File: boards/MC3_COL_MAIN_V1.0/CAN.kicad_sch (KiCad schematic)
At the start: 10 parts, among them J70 CAN, U70 TJA1051T/3

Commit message: User: re-annotated schematic (CAN/F412 parts), drill/place + grid origin at (100,100) saved in the board
Co-Authored-By: Claude Fable 5 <noreply@anthropic.com>
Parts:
- renumbered C70 to C28, C71 to C29, C72 to C30, D70 to D4, FB62 to FB3, J70 to J12, JP70 to JP1, R70 to R31, R71 to R32, U70 to U8

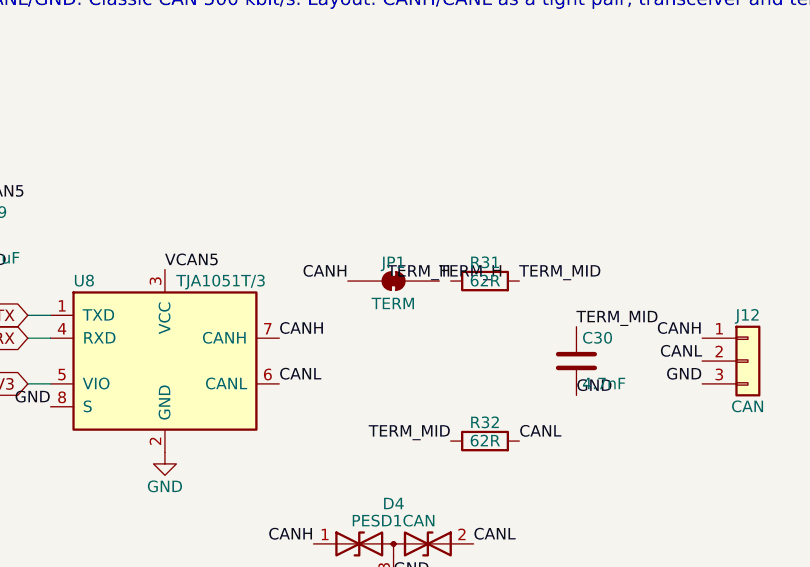
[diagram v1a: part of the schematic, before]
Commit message: CAN: termination enable is a fitted 0R (R72, C17168) instead of the bridged solder jumper (custom-pad footprint not placeable over KiCad 10 IPC)
Co-Authored-By: Claude Fable 5 <noreply@anthropic.com>
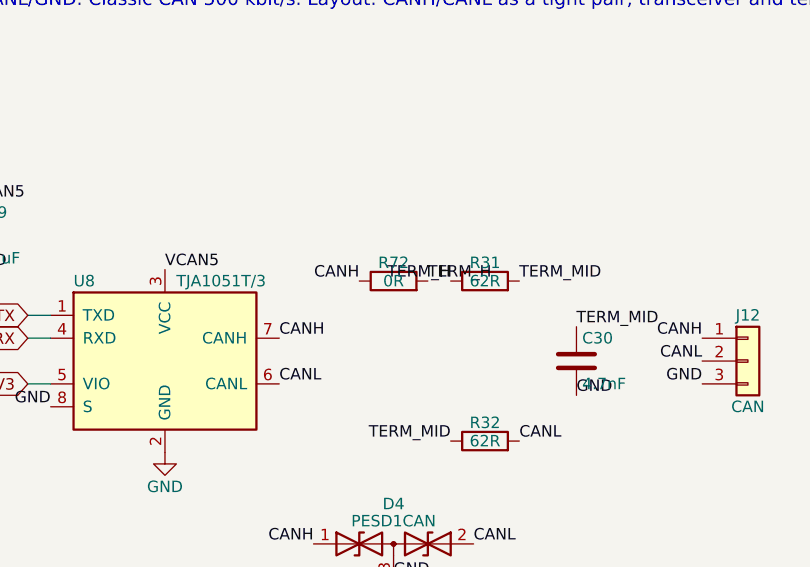
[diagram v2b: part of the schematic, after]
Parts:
- removed JP1: TERM, MC3_COL_MAIN:SolderJumper-2_P1.3mm_Bridged_RoundedPad1.0x1.5mm, symbol Jumper:SolderJumper_2_Bridged
- added R72: 0R, MC3_COL_MAIN:R_0402_1005Metric, symbol Device:R
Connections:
- net CANH: now also R72.1
- net TERM_H: now also R72.2
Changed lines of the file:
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@@
 	(generator_version "10.0")
 	(paper "A4")
-	(text "CAN - machine control link (decision 2026-08-22; vault Control Electronics open item). STM32F412 CAN1 (PA11 RX / PA12 TX) -> TJA1051T/3 -> split termination (2x62R + 4.7nF, solder-jumper JP70 bridged) + PESD1CAN -> pads CANH/CANL/GND. Classic CAN 500 kbit/s. Layout: CANH/CANL as a tight pair, transceiver and termination next to the pads, D70 nearest the pads."
-		(exclude_from_sim no)
-		(at 30 40 0)
-		(effects
-			(font
-				(size 1.5 1.5)
-			)
-		)
-	)
 	(wire
 		(pts
-			(xy 87.63 82.55) (xy 85.09 82.55)
+			(xy 87.63 82.55)
+			(xy 85.09 82.55)
 		)
 		(stroke
@@
 	(wire
 		(pts
-			(xy 87.63 77.47) (xy 85.09 77.47)
+			(xy 87.63 77.47)
+			(xy 85.09 77.47)
 		)
 		(stroke
@@
 	(wire
 		(pts
-			(xy 87.63 74.93) (xy 85.09 74.93)
+			(xy 87.63 74.93)
+			(xy 85.09 74.93)
 		)
 		(stroke
@@
 	(wire
 		(pts
-			(xy 60.96 57.15) (xy 60.96 54.61)
+			(xy 60.96 57.15)
+			(xy 60.96 54.61)
 		)
 		(stroke
@@
 		)
 	)
+	(text "CAN - machine control link (decision 2026-08-22; vault Control Electronics open item). STM32F412 CAN1 (PA11 RX / PA12 TX) -> TJA1051T/3 -> split termination (2x62R + 4.7nF, solder-jumper JP70 bridged) + PESD1CAN -> pads CANH/CANL/GND. Classic CAN 500 kbit/s. Layout: CANH/CANL as a tight pair, transceiver and termination next to the pads, D70 nearest the pads."
+		(at 30 40 0)
+		(effects
+			(font
+				(size 1.5 1.5)
+			)
+		)
+	)
 	(label "TERM_MID"
 		(at 139.7 71.12 0)
@@
 	)
 	(label "TERM_H"
-		(at 130.81 71.12 0)
-		(effects
-			(font
-				(size 1.27 1.27)
-			)
-			(justify left bottom)
-		)
-	)
-	(label "TERM_H"
 		(at 132.08 71.12 180)
 		(effects
@@
 	)
 	(label "CANH"
-		(at 120.65 71.12 180)
-		(effects
-			(font
-				(size 1.27 1.27)
-			)
-			(justify right bottom)
-		)
-	)
-	(label "CANH"
 		(at 116.84 100.33 180)
 		(effects
@@
 	(label "VCAN5"
 		(at 71.12 62.23 0)
+		(effects
+			(font
+				(size 1.27 1.27)
+			)
+			(justify left bottom)
+		)
+	)
+	(label "CANH"
+		(at 121.92 71.12 180)
+		(effects
+			(font
+				(size 1.27 1.27)
+			)
+			(justify right bottom)
+		)
+	)
+	(label "TERM_H"
+		(at 129.54 71.12 0)
 		(effects
 			(font
@@
 		(at 135.89 88.9 90)
 		(unit 1)
-		(body_style 1)
 		(exclude_from_sim no)
 		(in_bom yes)
 		(on_board yes)
-		(in_pos_files yes)
 		(dnp no)
 		(property "Reference" "R32"
@@
 			)
 		)
+		(body_style 1)
+		(in_pos_files yes)
 		(pin "1"
 		)
@@
 		(at 165.1 80.01 0)
 		(unit 1)
-		(body_style 1)
 		(exclude_from_sim no)
 		(in_bom yes)
 		(on_board yes)
-		(in_pos_files yes)
 		(dnp no)
 		(property "Reference" "J12"
@@
 			)
 		)
+		(body_style 1)
+		(in_pos_files yes)
 		(pin "1"
 		)
@@
 		(at 71.12 66.04 0)
 		(unit 1)
-		(body_style 1)
 		(exclude_from_sim no)
 		(in_bom yes)
 		(on_board yes)
-		(in_pos_files yes)
 		(dnp no)
 		(property "Reference" "C28"
@@
 			)
 		)
+		(body_style 1)
+		(in_pos_files yes)
 		(pin "1"
 		)
@@
 		(at 125.73 100.33 0)
 		(unit 1)
-		(body_style 1)
 		(exclude_from_sim no)
 		(in_bom yes)
 		(on_board yes)
-		(in_pos_files yes)
 		(dnp no)
 		(property "Reference" "D4"
@@
 			)
 		)
+		(body_style 1)
+		(in_pos_files yes)
 		(pin "3"
 		)
@@
 		(at 78.74 66.04 0)
 		(unit 1)
-		(body_style 1)
 		(exclude_from_sim no)
 		(in_bom yes)
 		(on_board yes)
-		(in_pos_files yes)
 		(dnp no)
 		(property "Reference" "C29"
@@
 			)
 		)
+		(body_style 1)
+		(in_pos_files yes)
 		(pin "1"
 		)
@@
 	)
 	(symbol
-		(lib_id "Jumper:SolderJumper_2_Bridged")
-		(at 125.73 71.12 0)
+		(lib_id "Device:FerriteBead")
+		(at 60.96 60.96 0)
 		(unit 1)
-		(body_style 1)
 		(exclude_from_sim no)
 		(in_bom yes)
 		(on_board yes)
-		(in_pos_files yes)
-		(dnp no)
-		(property "Reference" "JP1"
-			(at 125.73 69.088 0)
-			(show_name no)
-			(do_not_autoplace no)
-			(effects
-				(font
-					(size 1.27 1.27)
-				)
-			)
-		)
-		(property "Value" "TERM"
-			(at 125.73 73.66 0)
-			(show_name no)
-			(do_not_autoplace no)
-			(effects
-				(font
-					(size 1.27 1.27)
-				)
-			)
-		)
-		(property "Footprint" "MC3_COL_MAIN:SolderJumper-2_P1.3mm_Bridged_RoundedPad1.0x1.5mm"
-			(at 125.73 71.12 0)
-			(hide yes)
-			(show_name no)
-			(do_not_autoplace no)
-			(effects
-				(font
-					(size 1.27 1.27)
-				)
-			)
-		)
-		(property "Datasheet" ""
-			(at 125.73 71.12 0)
-			(hide yes)
-			(show_name no)
-			(do_not_autoplace no)
-			(effects
-				(font
-					(size 1.27 1.27)
-				)
-			)
-		)
-		(property "Description" ""
-			(at 125.73 71.12 0)
-			(show_name no)
-			(do_not_autoplace no)
-			(effects
-				(font
-					(size 1.27 1.27)
-				)
-			)
-		)
-		(property "Note" "Solder jumper, BRIDGED by default = 120R termination fitted. No part"
-			(at 125.73 71.12 0)
-			(hide yes)
-			(show_name no)
-			(do_not_autoplace no)
-			(effects
-				(font
-					(size 1.27 1.27)
-				)
-			)
-		)
-		(pin "1"
-		)
-		(pin "2"
-		)
-		(instances
-			(project "CAN"
-				(path "/3d434ce1-889d-46d1-8950-1c686d039f9f"
-					(reference "JP70")
-					(unit 1)
-				)
-			)
-			(project "MC3_COL_MAIN_V1.0"
-				(path "/7d5f4202-d55e-4c7b-a2df-dd599db38e48/d53768a6-e0ca-46e0-8386-8014881aa541"
-					(reference "JP1")
-					(unit 1)
-				)
-			)
-		)
-	)
-	(symbol
-		(lib_id "Device:FerriteBead")
-		(at 60.96 60.96 0)
-		(unit 1)
-		(body_style 1)
-		(exclude_from_sim no)
-		(in_bom yes)
-		(on_board yes)
-		(in_pos_files yes)
 		(dnp no)
 		(property "Reference" "FB3"
@@
 			)
 		)
+		(body_style 1)
+		(in_pos_files yes)
 		(pin "1"
 		)
@@
 		(at 135.89 71.12 90)
 		(unit 1)
-		(body_style 1)
 		(exclude_from_sim no)
 		(in_bom yes)
 		(on_board yes)
-		(in_pos_files yes)
 		(dnp no)
 		(property "Reference" "R31"
@@
 			)
 		)
+		(body_style 1)
+		(in_pos_files yes)
 		(pin "1"
 		)
@@
 		(at 146.05 80.01 0)
 		(unit 1)
-		(body_style 1)
 		(exclude_from_sim no)
 		(in_bom yes)
 		(on_board yes)
-		(in_pos_files yes)
 		(dnp no)
 		(property "Reference" "C30"
@@
 			)
 		)
+		(body_style 1)
+		(in_pos_files yes)
 		(pin "1"
 		)
@@
 		(at 100.33 90.17 0)
 		(unit 1)
-		(body_style 1)
 		(exclude_from_sim no)
 		(in_bom yes)
 		(on_board yes)
-		(in_pos_files yes)
 		(dnp no)
 		(property "Reference" "#PWR022"
@@
 			)
 		)
+		(body_style 1)
+		(in_pos_files yes)
 		(pin "1"
 		)
@@
 		(at 100.33 80.01 0)
 		(unit 1)
-		(body_style 1)
 		(exclude_from_sim no)
 		(in_bom yes)
 		(on_board yes)
-		(in_pos_files yes)
 		(dnp no)
 		(property "Reference" "U8"
@@
 			)
 		)
+		(body_style 1)
+		(in_pos_files yes)
 		(pin "1"
 		)
@@
 		(at 60.96 64.77 180)
 		(unit 1)
-		(body_style 1)
 		(exclude_from_sim no)
 		(in_bom yes)
 		(on_board yes)
-		(in_pos_files yes)
 		(dnp no)
 		(property "Reference" "#PWR021"
@@
 			)
 		)
+		(body_style 1)
+		(in_pos_files yes)
 		(pin "1"
 		)
@@
 					(unit 1)
 				)
+			)
+		)
+	)
+	(symbol
+		(lib_id "Device:R")
+		(at 125.73 71.12 90)
+		(unit 1)
+		(in_bom yes)
+		(on_board yes)
+		(dnp no)
+		(property "Reference" "R72"
+			(at 125.73 69.088 90)
+			(effects
+				(font
+					(size 1.27 1.27)
+				)
+			)
+		)
+		(property "Value" "0R"
+			(at 125.73 71.12 90)
+			(effects
+				(font
+					(size 1.27 1.27)
+				)
+			)
+		)
+		(property "Footprint" "MC3_COL_MAIN:R_0402_1005Metric"
+			(at 125.73 71.12 0)
+			(hide yes)
+			(effects
+				(font
+					(size 1.27 1.27)
+				)
+			)
+		)
+		(property "Datasheet" ""
+			(at 125.73 71.12 0)
+			(hide yes)
+			(effects
+				(font
+					(size 1.27 1.27)
+				)
+			)
+		)
+		(property "LCSC" "C17168"
+			(at 125.73 71.12 0)
+			(hide yes)
+			(effects
+				(font
+					(size 1.27 1.27)
+				)
+			)
+		)
+		(property "MPN" "0402WGF0000TCE"
+			(at 125.73 71.12 0)
+			(hide yes)
+			(effects
+				(font
+					(size 1.27 1.27)
+				)
+			)
+		)
+		(property "Note" "Termination enable: 0R fitted = 120R split termination in (board is a bus end on the bench). Remove to un-terminate if the board sits mid-bus. Replaces the bridged solder jumper (custom-pad footprint not placeable over IPC)"
+			(at 125.73 71.12 0)
+			(hide yes)
+			(effects
+				(font
+					(size 1.27 1.27)
+				)
+			)
+		)
+		(instances
+			(project "CAN"
+				(path "3d434ce1-889d-46d1-8950-1c686d039f9f"
+					(reference "R72")
+					(unit 1)
+				)
